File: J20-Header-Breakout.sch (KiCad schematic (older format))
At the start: 0 parts

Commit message: Added Components to J20Header Breakout
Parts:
- added P?: CONN_02X20, symbol CONN_02X20
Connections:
- net labels added: GPIO186, GPIO187, GPIO219, GPIO36, GPIO37, GPIO38, GPIO63, SCL, SDA
- wire segments 0 -> 70
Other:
- note added: "GPIO PINOUT"
- note added: "Jetson Dev Carrier J20 Header"
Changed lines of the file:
@@
 Comment4 ""
 $EndDescr
+$Comp
+L CONN_02X20 P?
+U 1 1 58CAB084
+P 4650 4000
+F 0 "P?" H 4650 5050 50  0000 C CNN
+F 1 "CONN_02X20" V 4650 4000 50  0000 C CNN
+F 2 "" H 4650 3050 50  0000 C CNN
+F 3 "" H 4650 3050 50  0000 C CNN
+	1    4650 4000
+	1    0    0    -1
+$EndComp
+Wire Wire Line
+	4400 3050 3850 3050
+Wire Wire Line
+	3600 3150 4400 3150
+Wire Wire Line
+	3450 3250 4400 3250
+Wire Wire Line
+	4400 3350 3850 3350
+Wire Wire Line
+	4400 3450 3850 3450
+Wire Wire Line
+	4400 3550 3850 3550
+Wire Wire Line
+	3050 3650 4400 3650
+Wire Wire Line
+	4400 3750 3850 3750
+Wire Wire Line
+	4400 3850 3850 3850
+Wire Wire Line
+	4400 3950 3850 3950
+Wire Wire Line
+	3850 4050 4400 4050
+Wire Wire Line
+	4400 4150 3850 4150
+Wire Wire Line
+	4400 4250 3850 4250
+Wire Wire Line
+	4400 4350 3850 4350
+Wire Wire Line
+	3050 4450 4400 4450
+Wire Wire Line
+	3250 4550 4400 4550
+Wire Wire Line
+	3400 4650 4400 4650
+Wire Wire Line
+	4400 4750 3850 4750
+Wire Wire Line
+	3550 4850 4400 4850
+Wire Wire Line
+	4400 4950 3850 4950
+Wire Wire Line
+	5450 3050 4900 3050
+Wire Wire Line
+	5450 3150 4900 3150
+Wire Wire Line
+	5450 3250 4900 3250
+Wire Wire Line
+	5450 3350 4900 3350
+Wire Wire Line
+	5450 3450 4900 3450
+Wire Wire Line
+	5450 3550 4900 3550
+Wire Wire Line
+	5450 3650 4900 3650
+Wire Wire Line
+	4900 3750 6300 3750
+Wire Wire Line
+	4900 3850 6500 3850
+Wire Wire Line
+	5450 3950 4900 3950
+Wire Wire Line
+	4900 4050 5450 4050
+Wire Wire Line
+	5450 4150 4900 4150
+Wire Wire Line
+	5450 4250 4900 4250
+Wire Wire Line
+	5450 4350 4900 4350
+Wire Wire Line
+	5450 4450 4900 4450
+Wire Wire Line
+	4900 4550 6700 4550
+Wire Wire Line
+	5450 4650 4900 4650
+Wire Wire Line
+	5450 4750 4900 4750
+Wire Wire Line
+	5450 4850 4900 4850
+Wire Wire Line
+	5450 4950 4900 4950
+Text Label 4150 3650 2    49   ~ 0
+GPIO38
+Text Label 5300 3750 2    49   ~ 0
+GPIO37
+Text Label 5300 3850 2    49   ~ 0
+GPIO187
+Text Label 4300 4450 2    49   ~ 0
+GPIO219
+Text Label 4300 4550 2    49   ~ 0
+GPIO186
+Text Label 4300 4650 2    49   ~ 0
+GPIO63
+Text Label 4300 4850 2    49   ~ 0
+GPIO187
+Text Label 5400 4550 2    49   ~ 0
+GPIO36
+Text Notes 5200 5250 2    49   ~ 0
+Jetson Dev Carrier J20 Header
+Wire Wire Line
+	3050 3650 3050 2750
+Wire Wire Line
+	3050 2750 6300 2750
+Wire Wire Line
+	6300 2750 6300 3100
+Wire Wire Line
+	6300 3100 8400 3100
+Wire Wire Line
+	6300 3750 6300 3300
+Wire Wire Line
+	6300 3300 8400 3300
+Wire Wire Line
+	6500 3850 6500 3500
+Wire Wire Line
+	6500 3500 8400 3500
+Wire Wire Line
+	6700 4550 6700 3700
+Wire Wire Line
+	6700 3700 8400 3700
+Wire Wire Line
+	3550 4850 3550 5500
+Wire Wire Line
+	3550 5500 6900 5500
+Wire Wire Line
+	6900 5500 6900 3900
+Wire Wire Line
+	6900 3900 8400 3900
+Wire Wire Line
+	3400 4650 3400 5650
+Wire Wire Line
+	3400 5650 7100 5650
+Wire Wire Line
+	7100 5650 7100 4100
+Wire Wire Line
+	7100 4100 8400 4100
+Wire Wire Line
+	3250 4550 3250 5800
+Wire Wire Line
+	3250 5800 7250 5800
+Wire Wire Line
+	7250 5800 7250 4300
+Wire Wire Line
+	7250 4300 8400 4300
+Wire Wire Line
+	3050 4450 3050 5950
+Wire Wire Line
+	3050 5950 7450 5950
+Wire Wire Line
+	7450 5950 7450 4450
+Wire Wire Line
+	7450 4450 8400 4450
+Text HLabel 8400 3100 2    49   BiDi ~ 0
+GPIO38
+Text HLabel 8400 3300 2    49   BiDi ~ 0
+GPIO37
+Text HLabel 8400 3500 2    49   BiDi ~ 0
+GPIO187
+Text HLabel 8400 3700 2    49   BiDi ~ 0
+GPIO36
+Text HLabel 8400 3900 2    49   BiDi ~ 0
+GPIO187
+Text HLabel 8400 4100 2    49   BiDi ~ 0
+GPIO63
+Text HLabel 8400 4300 2    49   BiDi ~ 0
+GPIO186
+Text HLabel 8400 4450 2    49   BiDi ~ 0
+GPIO219
+Text Label 4150 3150 2    49   ~ 0
+SDA
+Text Label 4150 3250 2    49   ~ 0
+SCL
+Wire Wire Line
+	3600 3150 3600 2150
+Wire Wire Line
+	3600 2150 8400 2150
+Wire Wire Line
+	3450 3250 3450 1950
+Wire Wire Line
+	3450 1950 8400 1950
+Text HLabel 8400 1950 2    49   BiDi ~ 0
+SCL
+Text HLabel 8400 2150 2    49   BiDi ~ 0
+SDA
+Text Notes 6400 1150 2    118  ~ 24
+GPIO PINOUT
 $EndSCHEMATC

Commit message: Rev 1 Schematics
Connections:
- net labels added: 3.3V, 5V, Audio-MCLK, GND, GPIO184, UART-RST, UART-RX, UART-TX
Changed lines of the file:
@@
 Sheet 3 5
 Title "GPIO Breakout"
-Date "2017-03-16"
+Date "2017-03-17"
 Rev "A"
 Comp "Advanced Visual Electronics"
@@
 GPIO37
 Text Label 5300 3850 2    49   ~ 0
-GPIO187
+GPIO184
 Text Label 4300 4450 2    49   ~ 0
 GPIO219
@@
 GPIO37
 Text HLabel 8400 3500 2    49   BiDi ~ 0
-GPIO187
+GPIO184
 Text HLabel 8400 3700 2    49   BiDi ~ 0
 GPIO36
@@
 Text Notes 6400 1150 2    118  ~ 24
 GPIO PINOUT
+Text Label 4000 3050 0    60   ~ 0
+3.3V
+Text Label 5050 3050 0    60   ~ 0
+5V
+Text Label 5050 3150 0    60   ~ 0
+5V
+Text Label 5050 3250 0    60   ~ 0
+GND
+Text Label 3850 3350 0    60   ~ 0
+Audio-MCLK
+Text Label 4000 3450 0    60   ~ 0
+GND
+Text Label 3900 3550 0    60   ~ 0
+UART-RST
+Text Label 4950 3350 0    60   ~ 0
+UART-TX
+Text Label 4950 3450 0    60   ~ 0
+UART-RX
 $EndSCHEMATC

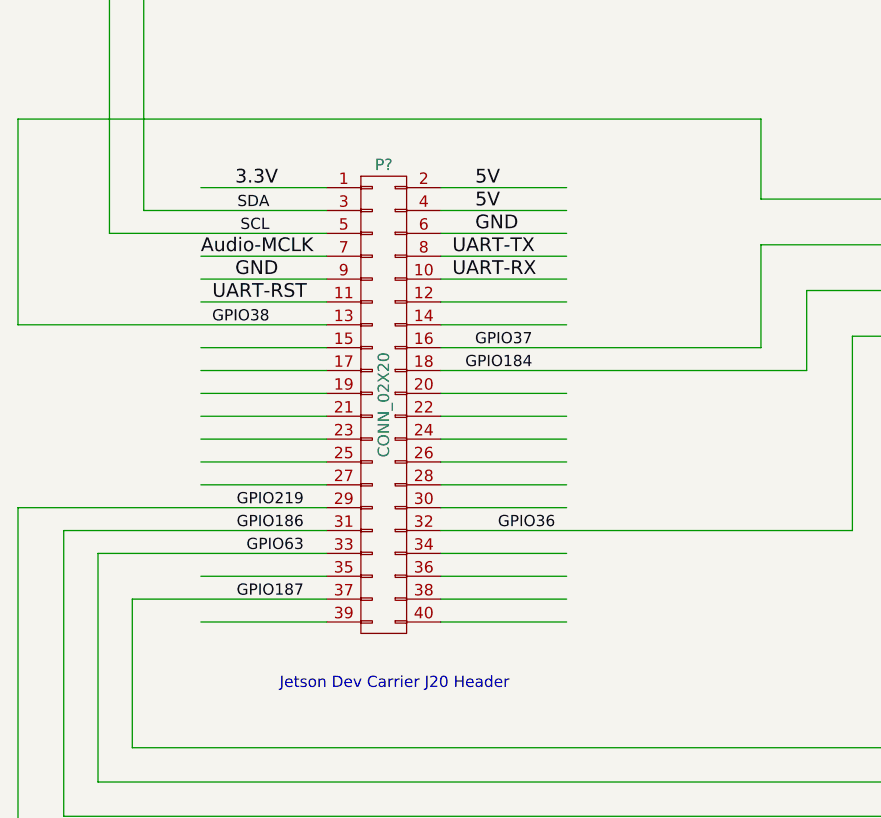
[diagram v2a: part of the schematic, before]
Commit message: More GPIO Pins Available
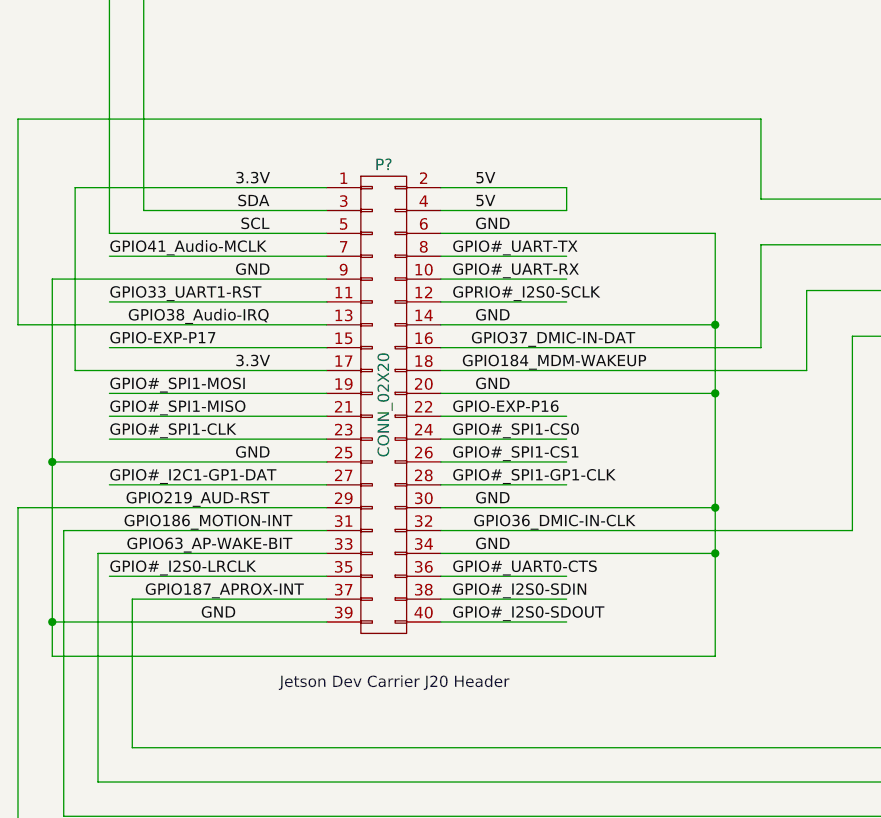
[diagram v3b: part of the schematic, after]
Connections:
- net labels added: GPIO#_I2C1-GP1-DAT, GPIO#_I2S0-LRCLK, GPIO#_I2S0-SDIN, GPIO#_I2S0-SDOUT, GPIO#_SPI1-CLK, GPIO#_SPI1-CS0, GPIO#_SPI1-CS1, GPIO#_SPI1-GP1-CLK, GPIO#_SPI1-MISO, GPIO#_SPI1-MOSI, GPIO#_UART-RX, GPIO#_UART-TX, GPIO#_UART0-CTS, GPIO-EXP-P16, GPIO-EXP-P17, GPIO184_MDM-WAKEUP, GPIO186_MOTION-INT, GPIO187_APROX-INT, GPIO219_AUD-RST, GPIO33_UART1-RST, GPIO36_DMIC-IN-CLK, GPIO37_DMIC-IN-DAT, GPIO38_Audio-IRQ, GPIO41_Audio-MCLK, GPIO63_AP-WAKE-BIT, GPRIO#_I2S0-SCLK
- net labels removed: Audio-MCLK, UART-RST, UART-RX, UART-TX
- wire segments 70 -> 75
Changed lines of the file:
@@
 $EndComp
 Wire Wire Line
-	4400 3050 3850 3050
+	3300 3050 4400 3050
 Wire Wire Line
 	3600 3150 4400 3150
@@
 	3450 3250 4400 3250
 Wire Wire Line
-	4400 3350 3850 3350
-Wire Wire Line
-	4400 3450 3850 3450
-Wire Wire Line
-	4400 3550 3850 3550
+	3450 3350 4400 3350
+Wire Wire Line
+	3200 3450 4400 3450
+Wire Wire Line
+	3450 3550 4400 3550
 Wire Wire Line
 	3050 3650 4400 3650
 Wire Wire Line
-	4400 3750 3850 3750
-Wire Wire Line
-	4400 3850 3850 3850
-Wire Wire Line
-	4400 3950 3850 3950
-Wire Wire Line
-	3850 4050 4400 4050
-Wire Wire Line
-	4400 4150 3850 4150
-Wire Wire Line
-	4400 4250 3850 4250
-Wire Wire Line
-	4400 4350 3850 4350
+	3450 3750 4400 3750
+Wire Wire Line
+	3450 3950 4400 3950
+Wire Wire Line
+	3450 4050 4400 4050
+Wire Wire Line
+	3450 4150 4400 4150
+Wire Wire Line
+	3200 4250 4400 4250
+Wire Wire Line
+	3450 4350 4400 4350
 Wire Wire Line
 	3050 4450 4400 4450
@@
 	3400 4650 4400 4650
 Wire Wire Line
-	4400 4750 3850 4750
+	3450 4750 4400 4750
 Wire Wire Line
 	3550 4850 4400 4850
 Wire Wire Line
-	4400 4950 3850 4950
+	3200 4950 4400 4950
 Wire Wire Line
 	5450 3050 4900 3050
@@
 	5450 3150 4900 3150
 Wire Wire Line
-	5450 3250 4900 3250
+	4900 3250 6100 3250
 Wire Wire Line
 	5450 3350 4900 3350
@@
 	5450 3550 4900 3550
 Wire Wire Line
-	5450 3650 4900 3650
+	4900 3650 6100 3650
 Wire Wire Line
 	4900 3750 6300 3750
@@
 	4900 3850 6500 3850
 Wire Wire Line
-	5450 3950 4900 3950
+	6100 3950 4900 3950
 Wire Wire Line
 	4900 4050 5450 4050
@@
 	5450 4350 4900 4350
 Wire Wire Line
-	5450 4450 4900 4450
+	6100 4450 4900 4450
 Wire Wire Line
 	4900 4550 6700 4550
 Wire Wire Line
-	5450 4650 4900 4650
+	6100 4650 4900 4650
 Wire Wire Line
 	5450 4750 4900 4750
@@
 	5450 4950 4900 4950
 Text Label 4150 3650 2    49   ~ 0
-GPIO38
-Text Label 5300 3750 2    49   ~ 0
-GPIO37
-Text Label 5300 3850 2    49   ~ 0
-GPIO184
-Text Label 4300 4450 2    49   ~ 0
-GPIO219
-Text Label 4300 4550 2    49   ~ 0
-GPIO186
-Text Label 4300 4650 2    49   ~ 0
-GPIO63
+GPIO38_Audio-IRQ
+Text Label 5750 3750 2    49   ~ 0
+GPIO37_DMIC-IN-DAT
+Text Label 5800 3850 2    49   ~ 0
+GPIO184_MDM-WAKEUP
+Text Label 4150 4450 2    49   ~ 0
+GPIO219_AUD-RST
+Text Label 4250 4550 2    49   ~ 0
+GPIO186_MOTION-INT
+Text Label 4250 4650 2    49   ~ 0
+GPIO63_AP-WAKE-BIT
 Text Label 4300 4850 2    49   ~ 0
-GPIO187
-Text Label 5400 4550 2    49   ~ 0
-GPIO36
+GPIO187_APROX-INT
+Text Label 5750 4550 2    49   ~ 0
+GPIO36_DMIC-IN-CLK
 Text Notes 5200 5250 2    49   ~ 0
 Jetson Dev Carrier J20 Header
@@
 Text Notes 6400 1150 2    118  ~ 24
 GPIO PINOUT
-Text Label 4000 3050 0    60   ~ 0
+Text Label 4000 3050 0    49   ~ 0
 3.3V
-Text Label 5050 3050 0    60   ~ 0
+Text Label 5050 3050 0    49   ~ 0
 5V
-Text Label 5050 3150 0    60   ~ 0
+Text Label 5050 3150 0    49   ~ 0
 5V
-Text Label 5050 3250 0    60   ~ 0
-GND
-Text Label 3850 3350 0    60   ~ 0
-Audio-MCLK
-Text Label 4000 3450 0    60   ~ 0
-GND
-Text Label 3900 3550 0    60   ~ 0
-UART-RST
-Text Label 4950 3350 0    60   ~ 0
-UART-TX
-Text Label 4950 3450 0    60   ~ 0
-UART-RX
+Text Label 5050 3250 0    49   ~ 0
+GND
+Text Label 3450 3350 0    49   ~ 0
+GPIO41_Audio-MCLK
+Text Label 4000 3450 0    49   ~ 0
+GND
+Text Label 3450 3550 0    49   ~ 0
+GPIO33_UART1-RST
+Text Label 4950 3350 0    49   ~ 0
+GPIO#_UART-TX
+Text Label 4950 3450 0    49   ~ 0
+GPIO#_UART-RX
+Text Label 3450 3750 0    49   ~ 0
+GPIO-EXP-P17
+Text Label 3450 3950 0    49   ~ 0
+GPIO#_SPI1-MOSI
+Text Label 3450 4050 0    49   ~ 0
+GPIO#_SPI1-MISO
+Text Label 3450 4150 0    49   ~ 0
+GPIO#_SPI1-CLK
+Text Label 4000 4250 0    49   ~ 0
+GND
+Text Label 3450 4350 0    49   ~ 0
+GPIO#_I2C1-GP1-DAT
+Text Label 4000 3850 0    49   ~ 0
+3.3V
+Text Label 3450 4750 0    49   ~ 0
+GPIO#_I2S0-LRCLK
+Text Label 3850 4950 0    49   ~ 0
+GND
+Text Label 4950 3550 0    49   ~ 0
+GPRIO#_I2S0-SCLK
+Text Label 5050 3650 0    49   ~ 0
+GND
+Text Label 5050 3950 0    49   ~ 0
+GND
+Text Label 4950 4050 0    49   ~ 0
+GPIO-EXP-P16
+Text Label 4950 4150 0    49   ~ 0
+GPIO#_SPI1-CS0
+Text Label 4950 4250 0    49   ~ 0
+GPIO#_SPI1-CS1
+Text Label 4950 4350 0    49   ~ 0
+GPIO#_SPI1-GP1-CLK
+Text Label 5050 4450 0    49   ~ 0
+GND
+Text Label 5050 4650 0    49   ~ 0
+GND
+Text Label 4950 4750 0    49   ~ 0
+GPIO#_UART0-CTS
+Text Label 4950 4850 0    49   ~ 0
+GPIO#_I2S0-SDIN
+Text Label 4950 4950 0    49   ~ 0
+GPIO#_I2S0-SDOUT
+Wire Wire Line
+	6100 3250 6100 5100
+Connection ~ 6100 3650
+Connection ~ 6100 3950
+Connection ~ 6100 4450
+Wire Wire Line
+	3200 3450 3200 5100
+Connection ~ 3200 4250
+Wire Wire Line
+	3200 5100 6100 5100
+Connection ~ 6100 4650
+Connection ~ 3200 4950
+Wire Wire Line
+	5450 3150 5450 3050
+Wire Wire Line
+	3300 3850 4400 3850
+Wire Wire Line
+	3300 3850 3300 3050
 $EndSCHEMATC

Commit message: Rev .99999 w/ Layout
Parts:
- P301: renamed from P?; footprint (none) -> Pin_Headers:Pin_Header_Straight_2x20_Pitch2.54mm
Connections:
- no-connect marks 0 -> 17
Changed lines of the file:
@@
 $EndDescr
 $Comp
-L CONN_02X20 P?
+L CONN_02X20 P301
 U 1 1 58CAB084
 P 4650 4000
-F 0 "P?" H 4650 5050 50  0000 C CNN
+F 0 "P301" H 4650 5050 50  0000 C CNN
 F 1 "CONN_02X20" V 4650 4000 50  0000 C CNN
-F 2 "" H 4650 3050 50  0000 C CNN
+F 2 "Pin_Headers:Pin_Header_Straight_2x20_Pitch2.54mm" H 4650 3050 50  0001 C CNN
 F 3 "" H 4650 3050 50  0000 C CNN
 	1    4650 4000
@@
 Wire Wire Line
 	3300 3850 3300 3050
+Text HLabel 5450 3050 2    60   Output ~ 0
+5V
+Text HLabel 3300 3050 0    60   Output ~ 0
+3.3V
+NoConn ~ 3450 3350
+NoConn ~ 3450 3550
+NoConn ~ 3450 3750
+NoConn ~ 3450 3950
+NoConn ~ 3450 4050
+NoConn ~ 3450 4150
+NoConn ~ 3450 4350
+NoConn ~ 5450 3350
+NoConn ~ 5450 3450
+NoConn ~ 5450 3550
+NoConn ~ 5450 4050
+NoConn ~ 5450 4150
+NoConn ~ 5450 4250
+NoConn ~ 5450 4350
+NoConn ~ 5450 4750
+NoConn ~ 5450 4850
+NoConn ~ 5450 4950
 $EndSCHEMATC
